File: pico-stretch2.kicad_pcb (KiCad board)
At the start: 4 copper layers, 82.1 x 21 mm, 66 parts, among them J2 Conn_01x03_Pin, J4 Conn_01x64_Castellated_Pads, U1 RP2350B_C42415655, U3 ME6217C33M5G, U4 W25Q128JVSIQTR, U5 RPI Radio Module 2, U6 APS6404L-3SQR, X1 ABM8-272-T3_C20625731

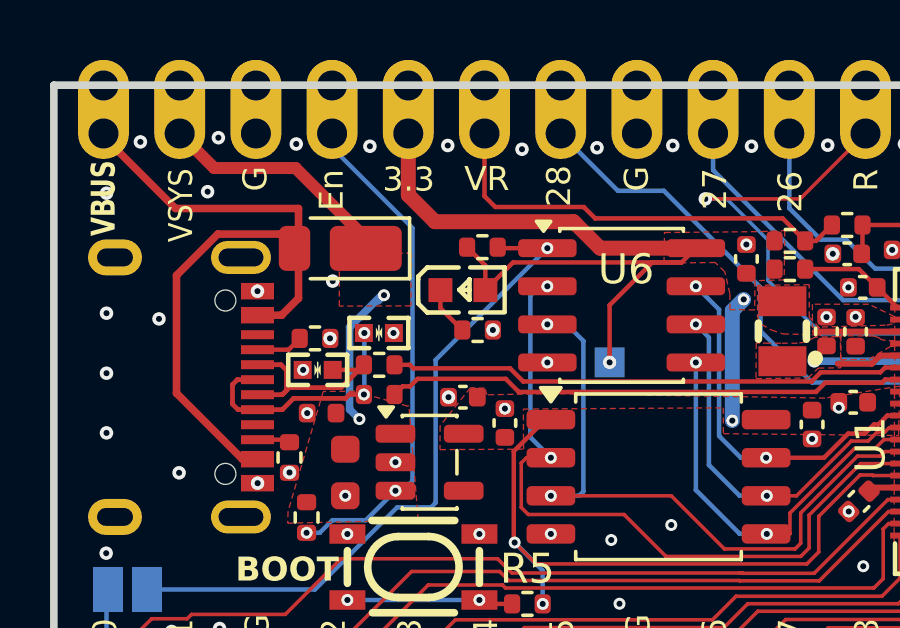
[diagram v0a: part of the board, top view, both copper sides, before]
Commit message: USB test pads, PSRAM CS on GPIO0 or GPIO47, back-side pin labels
- TP3 (USB D-) and TP4 (USB D+) on the back, connector side of R2/R3; new via in D2's signal pad for D-
- JP4 (back, beside U6) selects GPIO47 as the PSRAM chip select; JP1 still selects GPIO0. GPIO47 reaches
  JP4 on a 0.15 mm Inner2 track from castellated pad 44 along y 94.05 (back-layer traces only cross it,
  every via 0.42 mm or more away) and one via; JP4 sits at the PSRAM end so an open JP4 leaves no stub
- Every castellated pad labelled on the back (same text as the front); D-/D+ beside the test pads;
  jumper note moved off TP4 and rewritten for JP4; back logo moved down 2.9 mm to clear the labels
- README: PSRAM jumper choice, back-side notes
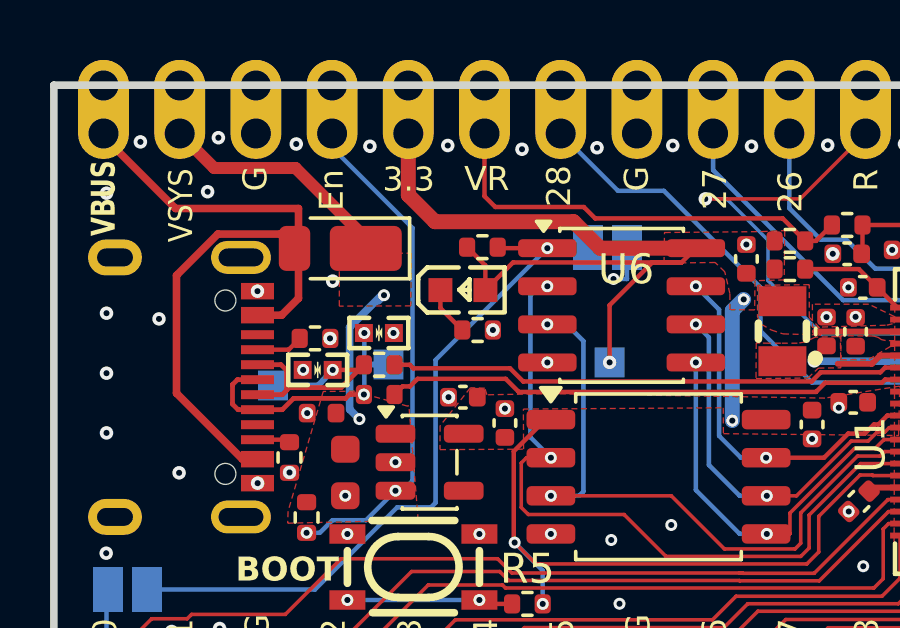
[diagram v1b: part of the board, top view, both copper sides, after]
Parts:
- added JP4: SolderJumper_2_Open, Jumper:SolderJumper-2_P1.3mm_Open_Pad1.0x1.5mm, B.Cu at (127.6, 96.4)
- added TP3: TestPoint, TestPoint:TestPoint_Pad_1.0x1.0mm, B.Cu at (116.5, 101.0)
- added TP4: TestPoint, TestPoint:TestPoint_Pad_1.0x1.0mm, B.Cu at (120.3, 100.3)
- moved G*** 3.07 mm to (172.2, 102.3)
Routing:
- net GPIO47/ADC7: track 25.9 -> 64.7 mm, vias 0 -> 1
- net USB2_D-: track 7.00 -> 9.22 mm, vias 0 -> 1
- net Net-(JP1-A): track 22.5 -> 23.9 mm
- net USB2_D+: track 8.28 -> 9.09 mm
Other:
- board text added: "D+"
- board text added: "D-"
- board text added: "PSRAM CS: JP1=GP0 or JP4=GP47 WIFI: JP2+JP3"
- board text removed: "JP1 PSRAM JP2/JP3 WIFI"

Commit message: Join JP4's GPIO47 link near U1 instead of at pad 44
The Inner2 link from JP4 ran 34 mm along y 94.05 to castellated pad 44, slitting
the Inner2 ground plane under ten back-side GPIO traces (GP16-22, GP26-28) and
crossing the Pico-footprint cut line. It now drops onto U1's GPIO47 front track at
its corner (139.26, 94.54): Inner2 run 37.3 -> 14.5 mm, crossed only by GP26-28,
and nothing crosses the cut line.

Also ignore KiCad's automatic project backups.
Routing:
- net GPIO47/ADC7: track 64.7 -> 41.9 mm, vias 1 -> 2
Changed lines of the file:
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@@
+		(net "GPIO47{slash}ADC7")
+	)
+	(via
+		(at 139.26 94.54)
+		(size 0.4)
+		(drill 0.2)
+		(layers "F.Cu" "B.Cu")
 		(net "GPIO47{slash}ADC7")
 	)
@@
 	)
 	(segment
+		(start 138.77 94.05)
+		(end 139.26 94.54)
+		(width 0.15)
+		(layer "In2.Cu")
+		(net "GPIO47{slash}ADC7")
+	)
+	(segment
 		(start 127.8 97.45)
 		(end 127.8 95)
@@
 	)
 	(segment
-		(start 161.6 93.4)
-		(end 161.6 93)
+		(start 128.75 94.05)
+		(end 138.77 94.05)
 		(width 0.15)
 		(layer "In2.Cu")
-		(net "GPIO47{slash}ADC7")
-	)
-	(segment
-		(start 128.75 94.05)
-		(end 160.95 94.05)
-		(width 0.15)
-		(layer "In2.Cu")
-		(net "GPIO47{slash}ADC7")
-	)
-	(segment
-		(start 160.95 94.05)
-		(end 161.6 93.4)
-		(width 0.15)
-		(layer "In2.Cu")
